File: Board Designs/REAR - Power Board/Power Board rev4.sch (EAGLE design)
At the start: 88 parts, among them X1 CONNECTOR-2, X2 CONNECTOR-6, X3 CONNECTOR-10MX150L_VERTICAL-10, X4 CONNECTOR-10MX150L_VERTICAL-10

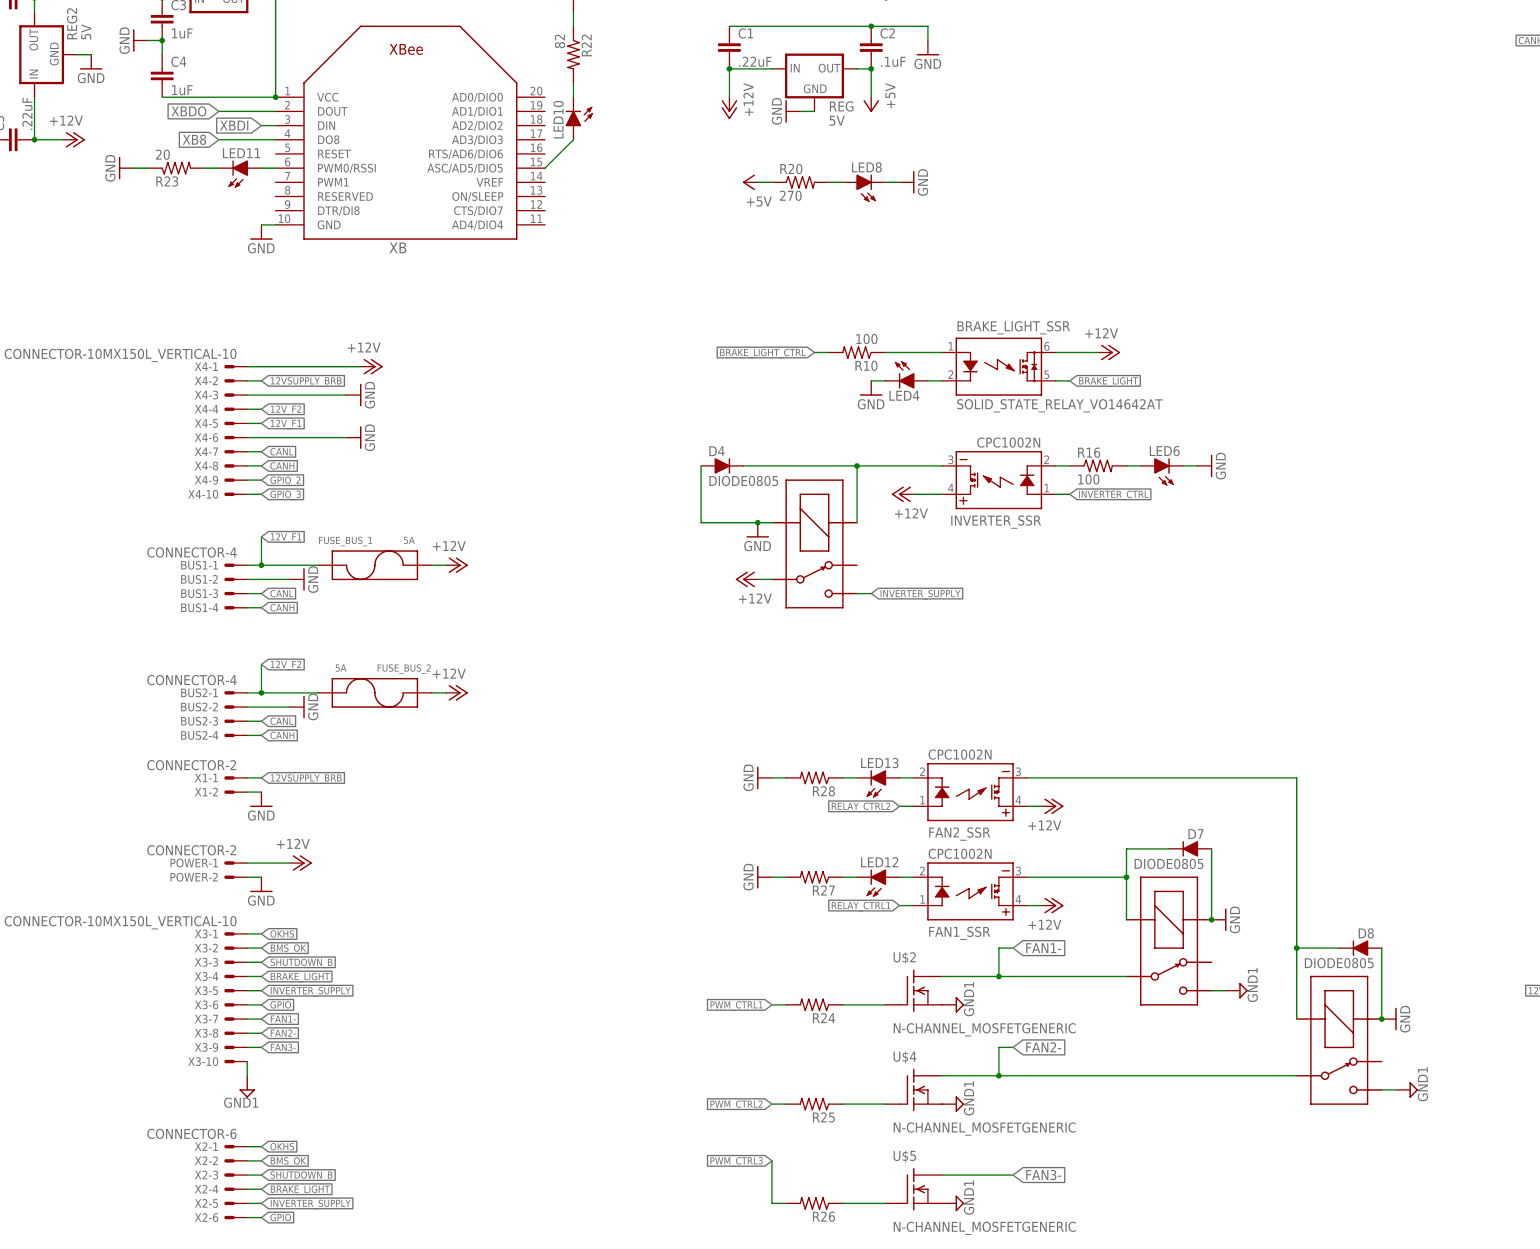
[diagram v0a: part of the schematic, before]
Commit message: Update TSAL in external diagram, power board gpio
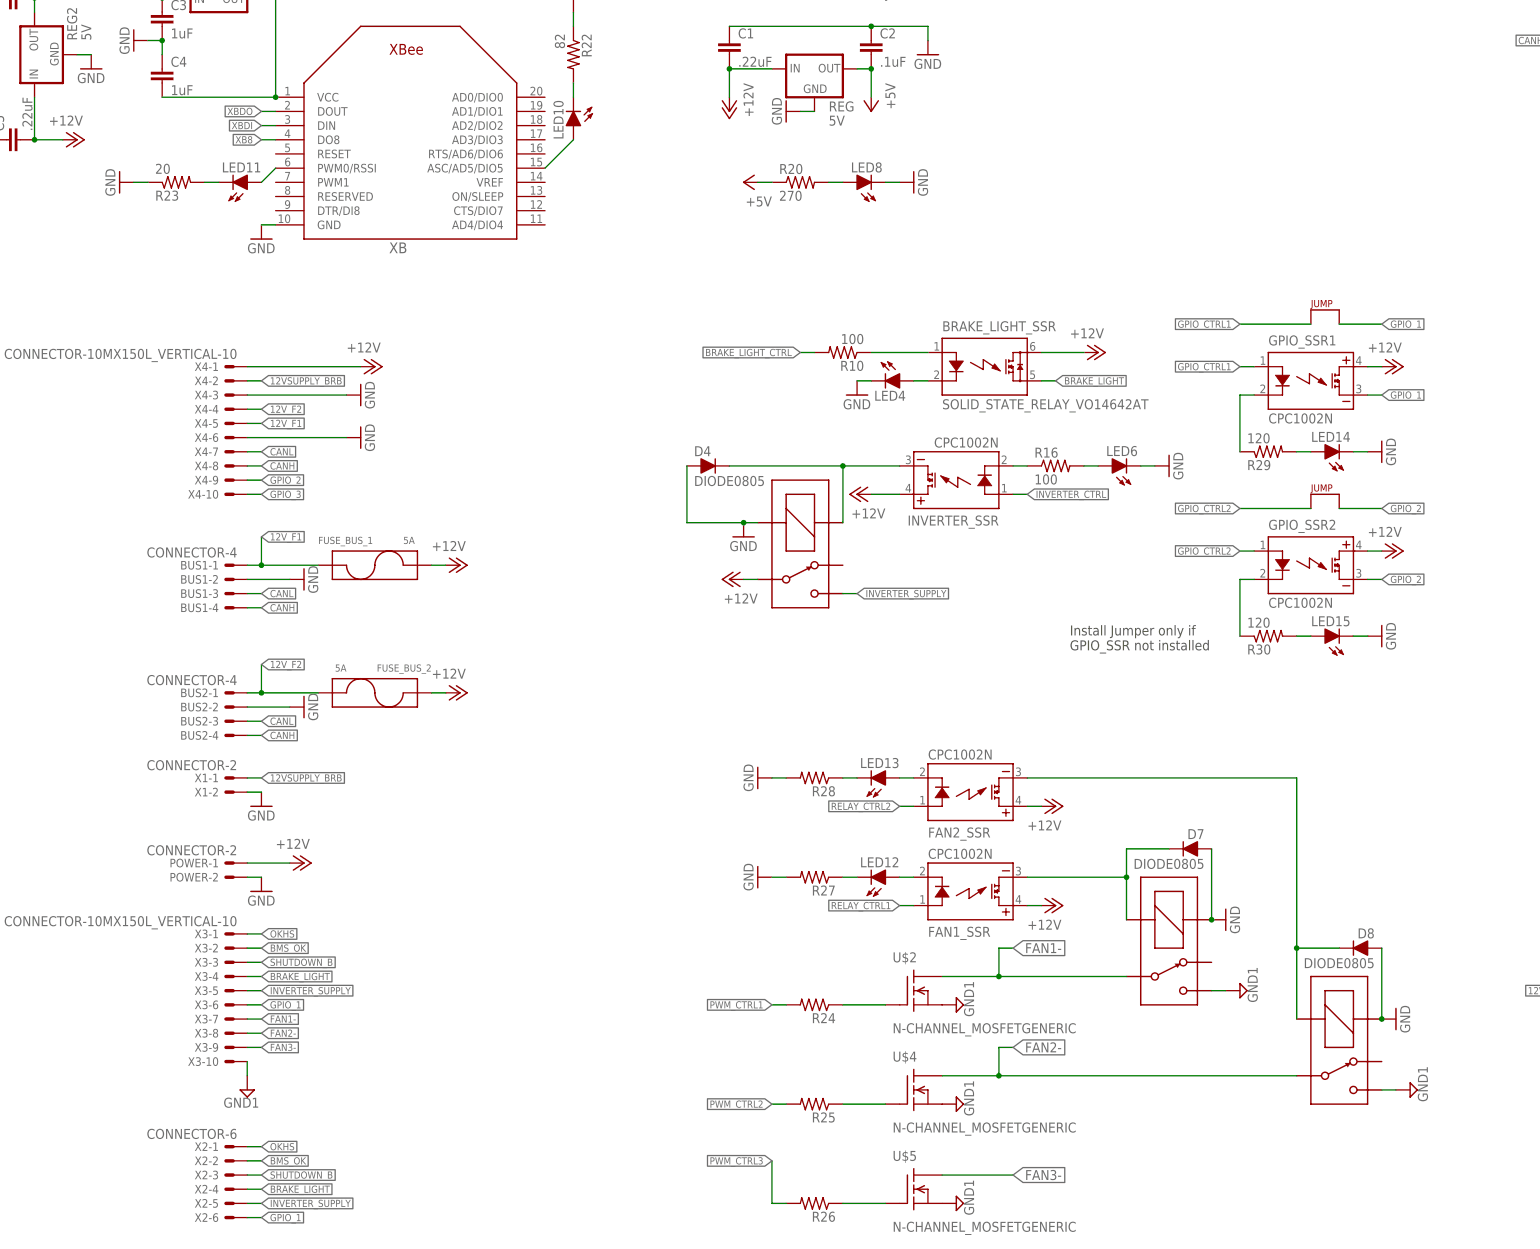
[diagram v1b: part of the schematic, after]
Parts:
- added GPIO_SSR1, GPIO_SSR2: CPC1002N, HyTechDevices:CPC1002N
- added LED14, LED15: (no value), HyTechDevices:LED-0805
- added R29, R30: 120, HyTechDevices:RESISTOR0805-RES
- added U$10, U$11: JUMPER.3, HyTechDevices:JUMPER.3
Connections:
- removed net GPIO: X2-6.S, X3-6.S
- new net GPIO_1: GPIO_SSR1.DC-, U$10.P$2, X2-6.S, X3-6.S
- new net N$13: LED14.A, R29.2
- new net N$14: LED15.A, R30.2
- new net N$6: GPIO_SSR1.CONTROL-, R29.1
- new net N$8: GPIO_SSR2.CONTROL-, R30.1
- net +12V: now also GPIO_SSR1.DC+, GPIO_SSR2.DC+
- net GND: now also LED14.C, LED15.C
- net GPIO_2: now also GPIO_SSR2.DC-, U$11.P$2
- net GPIO_CTRL1: now also GPIO_SSR1.CONTROL+, U$10.P$1
- net GPIO_CTRL2: now also GPIO_SSR2.CONTROL+, U$11.P$1
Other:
- note added: "Install Jumper only if GPIO_SSR not installed"
- moved on the sheet: BRAKE_LIGHT_SSR, D4, INVERTER_SSR, LED11, LED4, LED6, R10, R16, R23

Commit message: Update fuse holder size, add tactile smd button, update latching mechanism on rear ecu rev4
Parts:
- removed POWER: CONNECTOR-2, HyTechDevices:CONNECTOR-2
- removed R24, R25, R26: (no value), HyTechDevices:RESISTOR0805-RES
- added S1: (no value), HyTechDevices:BTN_10-XXSMD
- added U$8, U$9: MC34152, HyTechDevices:MC34152
- BOARD_TEMP: value THERMISTOR_NCP21 -> THERMISTOR_NCP210805; device HyTechDevices:THERMISTOR_NCP21 -> HyTechDevices:THERMISTOR_NCP210805
- LED10: value (none) -> Red
- LED11: value (none) -> Green
- LED8: value (none) -> Purple
- U$10, U$11: value JUMPER.3 -> JUMPER; device HyTechDevices:JUMPER.3 -> HyTechDevices:JUMPER
- renumbered FAN1_SSR to PUMP_SSR, FAN2_SSR to FAN_SSR
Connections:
- removed net FAN3-: U$5.D, X3-9.S
- removed net GPIO_3: X4-10.S
- new net LATCH_EXT_BUTTON: LED1.C, LED2.C, S1.P, S1.P1, X4-10.S
- new net PUMP1-: U$2.D, U$6.P, X3-7.S
- net +12V: now also FUSE_BUS_1.P1; no longer FUSE_BUS_1.P2, POWER-1.S
- net +5V: now also R12.2, R13.1, U$8.VCC, U$9.VCC
- net 12V_F1: now also FUSE_BUS_1.P2; no longer FUSE_BUS_1.P1
- net BMS_LATCH_CTRL: no longer R13.1
- net FAN1-: now also U$4.D, U$7.P, X3-8.S; no longer U$2.D, U$6.P, X3-7.S
- net FAN2-: now also U$5.D, X3-9.S; no longer U$4.D, U$7.P, X3-8.S
- net GND: now also S1.S, S1.S1, U$8.GND, U$9.GND; no longer LED1.C, LED2.C, POWER-2.S
- net IMD_LATCH_CTRL: no longer R12.2
- net N$39: now also U$8.OUT_A; no longer R24.1
- net N$40: now also U$8.OUT_B; no longer R25.1
- net N$41: now also U$9.OUT_B; no longer R26.1
- net PWM_CTRL1: now also U$8.IN_A; no longer R24.2
- net PWM_CTRL2: now also U$8.IN_B; no longer R25.2
- net PWM_CTRL3: now also U$9.IN_B; no longer R26.2
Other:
- moved on the sheet: LED10, R22, U$2, U$4, U$5, X2-1, X2-2, X2-3, X2-4, X2-5, X2-6, X3-1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

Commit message: Final tweaks to rear ECU rev4
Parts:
- LED1, LED2: value (none) -> White
- LED12, LED13, LED14, LED15, LED4, LED6: value (none) -> Red
- LED3, LED7: value (none) -> Green
- LED5, LED9: value (none) -> Yellow
- R10, R11, R16: value 100 -> 43
- R12, R13: value 100 -> 33
- R21: value 680 -> 820
- R22: value 82 -> 100
- R23: value 20 -> 33
- R27, R28: value (none) -> 33
- R29, R30: value 120 -> 43
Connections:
- removed net BMS_LATCH_CTRL: U$3.D11
- removed net IMD_LATCH_CTRL: U$3.D8(TX3)
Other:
- moved on the sheet: GPIO_SSR1, GPIO_SSR2, LED14, LED5, LED7, LED8, R11, R13, R14, R17, R18, R19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

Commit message: Add Rear ECU fuse to switch between FH and FSAE configuration, add shutdown circuit 5A fuse
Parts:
- added FSAE_FUSE: 8A, HyTechDevices:FUSE_MINIBLADE
- added SHUTDWN_FUSE: 5A, HyTechDevices:FUSE_MINIBLADE
- FH_FUSE: value 5A -> 8A
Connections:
- new net 12VSUPPLY_FSAE: FSAE_FUSE.P2, X4-1.S
- new net SHUTDOWN_C: D3.A, IMD_SHUTDOWN1.5, X2-3.S, X3-3.S
- net +12V: now also FSAE_FUSE.P1; no longer X4-1.S
- net 12VSUPPLY_BRB: now also SHUTDWN_FUSE.P2; no longer IMD_SHUTDOWN.6
- net SHUTDOWN_A: now also IMD_SHUTDOWN.6, SHUTDWN_FUSE.P1; no longer IMD_SHUTDOWN.5, IMD_SHUTDOWN1.6
- net SHUTDOWN_B: now also IMD_SHUTDOWN.5, IMD_SHUTDOWN1.6; no longer D3.A, IMD_SHUTDOWN1.5, X2-3.S, X3-3.S
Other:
- note added: "Install FH_FUSE for Formula Hybrid"
- note added: "Install FSAE_FUSE for FSAE"
- note removed: "Install fuse for Formula Hybrid"
- moved on the sheet: FH_FUSE, LED8, R20
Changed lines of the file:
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@@
 <part name="X3" library="HyTechDevices" deviceset="CONNECTOR-10" device="MX150L_VERTICAL-10"/>
 <part name="X4" library="HyTechDevices" deviceset="CONNECTOR-10" device="MX150L_VERTICAL-10"/>
-<part name="P+15" library="supply1" deviceset="+12V" device=""/>
 <part name="GND32" library="HyTechSymbols" deviceset="GND" device=""/>
 <part name="GND33" library="HyTechSymbols" deviceset="GND" device=""/>
@@
 <part name="GND39" library="HyTechSymbols" deviceset="GND" device=""/>
 <part name="P+19" library="supply1" deviceset="+12V" device=""/>
-<part name="FH_FUSE" library="HyTechDevices" deviceset="FUSE" device="_MINIBLADE" value="5A"/>
+<part name="FH_FUSE" library="HyTechDevices" deviceset="FUSE" device="_MINIBLADE" value="8A"/>
 <part name="P+18" library="supply1" deviceset="+12V" device=""/>
 <part name="P+20" library="supply1" deviceset="+12V" device=""/>
@@
 <part name="S1" library="HyTechDevices" deviceset="BTN_10-XX" device="SMD"/>
 <part name="GND2" library="HyTechSymbols" deviceset="GND" device=""/>
+<part name="FSAE_FUSE" library="HyTechDevices" deviceset="FUSE" device="_MINIBLADE" value="8A"/>
+<part name="P+7" library="supply1" deviceset="+12V" device=""/>
+<part name="SHUTDWN_FUSE" library="HyTechDevices" deviceset="FUSE" device="_MINIBLADE" value="5A"/>
 </parts>
 <sheets>
 <sheet>
 <plain>
-<text x="137.16" y="220.98" size="1.778" layer="97">Install fuse for Formula Hybrid</text>
-<wire x1="0" y1="162.56" x2="93.98" y2="162.56" width="0.1524" layer="90"/>
-<wire x1="93.98" y1="162.56" x2="93.98" y2="0" width="0.1524" layer="90"/>
-<wire x1="93.98" y1="0" x2="0" y2="0" width="0.1524" layer="90"/>
+<text x="149.86" y="220.98" size="1.778" layer="97">Install FH_FUSE for Formula Hybrid</text>
+<wire x1="0" y1="162.56" x2="96.52" y2="162.56" width="0.1524" layer="90"/>
+<wire x1="96.52" y1="162.56" x2="96.52" y2="0" width="0.1524" layer="90"/>
+<wire x1="96.52" y1="0" x2="0" y2="0" width="0.1524" layer="90"/>
 <wire x1="0" y1="0" x2="0" y2="162.56" width="0.1524" layer="90"/>
 <text x="0" y="162.56" size="5.08" layer="90">Connectors</text>
@@
 <wire x1="127" y1="-5.08" x2="127" y2="91.44" width="0.1524" layer="90"/>
 <text x="127" y="91.44" size="5.08" layer="90">Cooling</text>
-<wire x1="127" y1="238.76" x2="236.22" y2="238.76" width="0.1524" layer="90"/>
-<wire x1="236.22" y1="238.76" x2="236.22" y2="190.5" width="0.1524" layer="90"/>
-<wire x1="236.22" y1="190.5" x2="127" y2="190.5" width="0.1524" layer="90"/>
+<wire x1="127" y1="238.76" x2="251.46" y2="238.76" width="0.1524" layer="90"/>
+<wire x1="251.46" y1="238.76" x2="251.46" y2="190.5" width="0.1524" layer="90"/>
+<wire x1="251.46" y1="190.5" x2="127" y2="190.5" width="0.1524" layer="90"/>
 <wire x1="127" y1="190.5" x2="127" y2="238.76" width="0.1524" layer="90"/>
 <text x="127" y="238.76" size="5.08" layer="90">Power</text>
@@
 <text x="198.12" y="104.14" size="1.778" layer="97">Install Jumper only if
 GPIO_SSR not installed</text>
+<text x="205.74" y="220.98" size="1.778" layer="97">Install FSAE_FUSE for FSAE</text>
 </plain>
 <instances>
@@
 <instance part="C1" gate="G$1" x="137.16" y="210.82"/>
 <instance part="C2" gate="G$1" x="162.56" y="210.82"/>
-<instance part="GND7" gate="1" x="172.72" y="210.82"/>
+<instance part="GND7" gate="1" x="172.72" y="215.9" rot="R90"/>
 <instance part="U$1" gate="G$1" x="147.32" y="132.08" rot="R270"/>
 <instance part="GND8" gate="1" x="139.7" y="124.46"/>
@@
 <instance part="R18" gate="G$1" x="335.28" y="116.84" rot="R90"/>
 <instance part="GND22" gate="1" x="335.28" y="127" rot="R180"/>
-<instance part="LED8" gate="LED" x="210.82" y="215.9" rot="R90"/>
-<instance part="R20" gate="G$1" x="200.66" y="215.9"/>
-<instance part="GND23" gate="1" x="220.98" y="215.9" rot="R90"/>
-<instance part="P+6" gate="1" x="190.5" y="215.9" rot="R90"/>
+<instance part="LED8" gate="LED" x="223.52" y="198.12" rot="R90"/>
+<instance part="R20" gate="G$1" x="213.36" y="198.12"/>
+<instance part="GND23" gate="1" x="233.68" y="198.12" rot="R90"/>
+<instance part="P+6" gate="1" x="203.2" y="198.12" rot="R90"/>
 <instance part="IMD_SSR" gate="G$1" x="304.8" y="104.14" rot="MR0"/>
 <instance part="LED9" gate="LED" x="330.2" y="101.6" rot="R90"/>
@@
 <instance part="X4" gate="-9" x="48.26" y="134.62" rot="MR0"/>
 <instance part="X4" gate="-10" x="48.26" y="132.08" rot="MR0"/>
-<instance part="P+15" gate="1" x="73.66" y="154.94" rot="R270"/>
 <instance part="GND32" gate="1" x="71.12" y="149.86" rot="R90"/>
 <instance part="GND33" gate="1" x="71.12" y="142.24" rot="R90"/>
@@
 <instance part="GND39" gate="1" x="10.16" y="231.14" rot="R90"/>
 <instance part="P+19" gate="1" x="20.32" y="195.58" rot="R270"/>
-<instance part="FH_FUSE" gate="G$1" x="152.4" y="228.6"/>
-<instance part="P+18" gate="1" x="134.62" y="228.6" rot="MR270"/>
+<instance part="FH_FUSE" gate="G$1" x="162.56" y="228.6" rot="MR0"/>
+<instance part="P+18" gate="1" x="180.34" y="228.6" rot="R270"/>
 <instance part="P+20" gate="1" x="88.9" y="119.38" rot="R270"/>
 <instance part="P+21" gate="1" x="88.9" y="96.52" rot="R270"/>
@@
 <instance part="S1" gate="1" x="375.92" y="119.38" rot="R270"/>
 <instance part="GND2" gate="1" x="388.62" y="119.38" rot="R90"/>
+<instance part="FSAE_FUSE" gate="G$1" x="218.44" y="228.6" rot="MR0"/>
+<instance part="P+7" gate="1" x="236.22" y="228.6" rot="R270"/>
+<instance part="SHUTDWN_FUSE" gate="G$1" x="218.44" y="210.82" rot="MR0"/>
 </instances>
 <busses>
@@
 <pinref part="C2" gate="G$1" pin="1"/>
 <wire x1="137.16" y1="215.9" x2="162.56" y2="215.9" width="0.1524" layer="91"/>
-<wire x1="162.56" y1="215.9" x2="172.72" y2="215.9" width="0.1524" layer="91"/>
-<wire x1="172.72" y1="215.9" x2="172.72" y2="213.36" width="0.1524" layer="91"/>
+<wire x1="162.56" y1="215.9" x2="170.18" y2="215.9" width="0.1524" layer="91"/>
 <junction x="162.56" y="215.9"/>
 <pinref part="GND7" gate="1" pin="GND"/>
@@
 <pinref part="LED8" gate="LED" pin="C"/>
 <pinref part="GND23" gate="1" pin="GND"/>
-<wire x1="218.44" y1="215.9" x2="215.9" y2="215.9" width="0.1524" layer="91"/>
+<wire x1="231.14" y1="198.12" x2="228.6" y2="198.12" width="0.1524" layer="91"/>
 </segment>
 <segment>
@@
 </segment>
 </net>
-<net name="SHUTDOWN_B" class="0">
+<net name="SHUTDOWN_C" class="0">
 <segment>
 <pinref part="IMD_SHUTDOWN1" gate="G$1" pin="5"/>
@@
 </segment>
 </net>
-<net name="SHUTDOWN_A" class="0">
+<net name="SHUTDOWN_B" class="0">
 <segment>
 <pinref part="IMD_SHUTDOWN1" gate="G$1" pin="6"/>
@@
 <pinref part="R20" gate="G$1" pin="1"/>
 <pinref part="P+6" gate="1" pin="+5V"/>
-<wire x1="195.58" y1="215.9" x2="193.04" y2="215.9" width="0.1524" layer="91"/>
+<wire x1="208.28" y1="198.12" x2="205.74" y2="198.12" width="0.1524" layer="91"/>
 </segment>
 <segment>
@@
 <pinref part="LED8" gate="LED" pin="A"/>
 <pinref part="R20" gate="G$1" pin="2"/>
-<wire x1="205.74" y1="215.9" x2="208.28" y2="215.9" width="0.1524" layer="91"/>
+<wire x1="218.44" y1="198.12" x2="220.98" y2="198.12" width="0.1524" layer="91"/>
 </segment>
 </net>
@@
 </segment>
 <segment>
-<pinref part="X4" gate="-1" pin="S"/>
-<pinref part="P+15" gate="1" pin="+12V"/>
-<wire x1="71.12" y1="154.94" x2="50.8" y2="154.94" width="0.1524" layer="91"/>
-</segment>
-<segment>
 <pinref part="FAN_SSR" gate="G$1" pin="DC+"/>
 <pinref part="P+16" gate="1" pin="+12V"/>
@@
 <pinref part="FH_FUSE" gate="G$1" pin="P1"/>
 <pinref part="P+18" gate="1" pin="+12V"/>
-<wire x1="137.16" y1="228.6" x2="142.24" y2="228.6" width="0.1524" layer="91"/>
+<wire x1="177.8" y1="228.6" x2="172.72" y2="228.6" width="0.1524" layer="91"/>
 </segment>
 <segment>
@@
 <wire x1="83.82" y1="119.38" x2="86.36" y2="119.38" width="0.1524" layer="91"/>
 </segment>
+<segment>
+<pinref part="FSAE_FUSE" gate="G$1" pin="P1"/>
+<wire x1="228.6" y1="228.6" x2="233.68" y2="228.6" width="0.1524" layer="91"/>
+<pinref part="P+7" gate="1" pin="+12V"/>
+</segment>
 </net>
 <net name="12VSUPPLY_BRB" class="0">
-<segment>
-<pinref part="IMD_SHUTDOWN" gate="G$1" pin="6"/>
-<label x="294.64" y="43.18" size="1.27" layer="95" rot="R180" xref="yes"/>
-<wire x1="297.18" y1="43.18" x2="294.64" y2="43.18" width="0.1524" layer="91"/>
-</segment>
 <segment>
 <pinref part="X4" gate="-2" pin="S"/>
@@
 <segment>
 <pinref part="FH_FUSE" gate="G$1" pin="P2"/>
-<wire x1="162.56" y1="228.6" x2="165.1" y2="228.6" width="0.1524" layer="91"/>
-<label x="165.1" y="228.6" size="1.27" layer="95" xref="yes"/>
+<wire x1="152.4" y1="228.6" x2="149.86" y2="228.6" width="0.1524" layer="91"/>
+<label x="149.86" y="228.6" size="1.27" layer="95" rot="MR0" xref="yes"/>
+</segment>
+<segment>
+<pinref part="SHUTDWN_FUSE" gate="G$1" pin="P2"/>
+<wire x1="208.28" y1="210.82" x2="205.74" y2="210.82" width="0.1524" layer="91"/>
+<label x="205.74" y="210.82" size="1.27" layer="95" rot="MR0" xref="yes"/>
 </segment>
 </net>
@@
 </segment>
 </net>
+<net name="12VSUPPLY_FSAE" class="0">
+<segment>
+<pinref part="FSAE_FUSE" gate="G$1" pin="P2"/>
+<wire x1="208.28" y1="228.6" x2="205.74" y2="228.6" width="0.1524" layer="91"/>
+<label x="205.74" y="228.6" size="1.27" layer="95" rot="MR0" xref="yes"/>
+</segment>
+<segment>
+<pinref part="X4" gate="-1" pin="S"/>
+<wire x1="53.34" y1="154.94" x2="50.8" y2="154.94" width="0.1524" layer="91"/>
+<label x="53.34" y="154.94" size="1.27" layer="95" xref="yes"/>
+</segment>
+</net>
+<net name="SHUTDOWN_A" class="0">
+<segment>
+<pinref part="IMD_SHUTDOWN" gate="G$1" pin="6"/>
+<label x="294.64" y="43.18" size="1.27" layer="95" rot="R180" xref="yes"/>
+<wire x1="297.18" y1="43.18" x2="294.64" y2="43.18" width="0.1524" layer="91"/>
+</segment>
+<segment>
+<pinref part="SHUTDWN_FUSE" gate="G$1" pin="P1"/>
+<wire x1="228.6" y1="210.82" x2="231.14" y2="210.82" width="0.1524" layer="91"/>
+<label x="231.14" y="210.82" size="1.27" layer="95" rot="MR180" xref="yes"/>
+</segment>
+</net>
